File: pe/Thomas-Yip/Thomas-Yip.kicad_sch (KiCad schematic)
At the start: 17 parts, among them U1 TPS563201

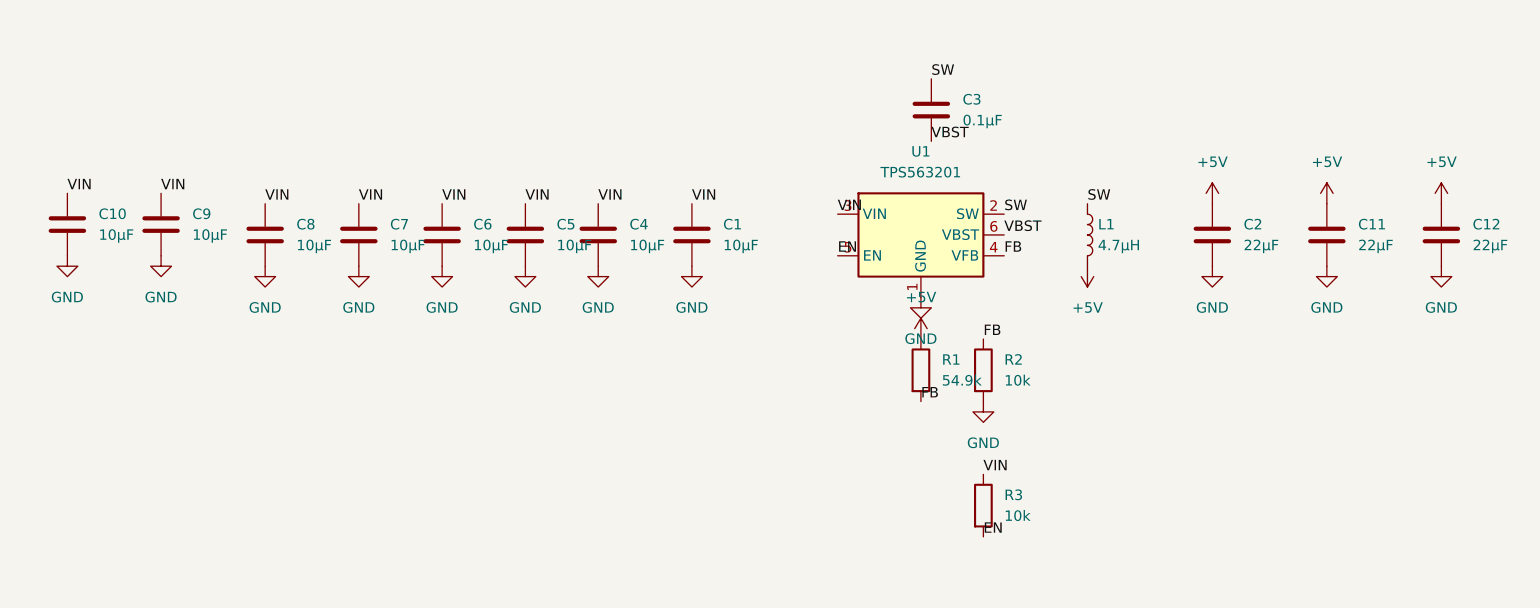
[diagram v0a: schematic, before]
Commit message: Complete buck converter schematic
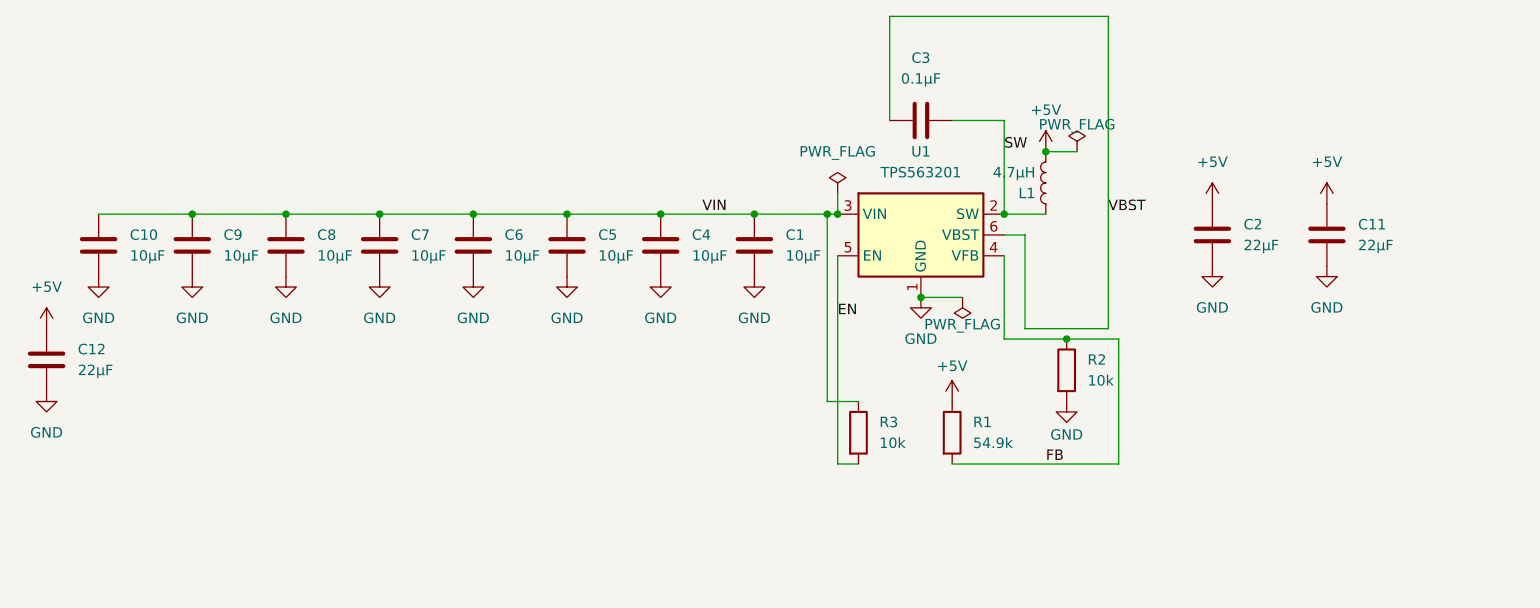
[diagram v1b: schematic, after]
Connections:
- net SW: now also C3.2; no longer C3.1
- net VBST: now also C3.1; no longer C3.2
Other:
- moved on the sheet: C1, C10, C12, C3, C4, C5, C6, C7, C8, C9, L1, R1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

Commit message: Added onboarding document link
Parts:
- L1: value 4.7µH -> LSDND5050PKT4R7M
- U1: value TPS563201 -> TPS563201DDCR
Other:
- note added: "Power Electronics Onboarding Google Doc"
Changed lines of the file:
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@@
 		(comment 3 "${COMMENT2}")
 	)
+	(text "Power Electronics Onboarding Google Doc"
+		(exclude_from_sim no)
+		(at 77.978 79.502 0)
+		(effects
+			(font
+				(size 1.27 1.27)
+			)
+			(href "https://docs.google.com/document/d/1iW4MuP0Th3IQ3AF9iYU6Qq7mVLO3Fhc-mOpD14-F57k/edit?tab=t.0")
+		)
+	)
 	(junction
 		(at 91.44 93.98)
@@
 			)
 		)
-		(property "Value" "TPS563201"
+		(property "Value" "TPS563201DDCR"
 			(at 123.19 88.9 0)
 			(show_name no)
@@
 			)
 		)
-		(property "Value" "4.7µH"
+		(property "Value" "LSDND5050PKT4R7M"
 			(at 137.16 88.9001 0)
 			(show_name no)

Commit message: Update Thomas-Yip.kicad_sch
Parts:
- L1: value LSDND5050PKT4R7M -> 4.7µF
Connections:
- net EN: now also R3.1; no longer R3.2
- net SW: now also C3.1; no longer C3.2
- net VBST: now also C3.2; no longer C3.1
- net VIN: now also R3.2; no longer R3.1
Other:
- moved on the sheet: C1, C10, C11, C12, C2, C3, C4, C5, C6, C7, C8, C9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

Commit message: Final Buck Converter
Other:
- title: ${BOARD_TITLE} -> Finalized Buck Converter
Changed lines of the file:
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@@
 	(paper "A")
 	(title_block
-		(title "${BOARD_TITLE}")
-		(date "${CURRENT_DATE}")
-		(rev "${REVISION}")
+		(title "Finalized Buck Converter")
+		(date "2026-10-16")
+		(rev "1.0")
 		(company "Formula Slug")
-		(comment 1 "${NAMES}")
-		(comment 2 "${COMMENT1}")
-		(comment 3 "${COMMENT2}")
+		(comment 1 "Thomas Yip")
+		(comment 2 "I accidently did all my commits on a fork, so commit dates are the same")
+		(comment 3 "Input capacitors drop from 10µF to ~1.8, so I needed 8 of them")
 	)
 	(text "Power Electronics Onboarding Google Doc"
